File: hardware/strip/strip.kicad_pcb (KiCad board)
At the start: 4 copper layers, 66 x 18 mm, 43 parts, among them J105 CORTEX-DEBUG, J106 JAE_DX07S016JA3, J301 WAGO-2065, J302 WAGO-2065, J303 WAGO-2065, SW101 SW_Push, SW102 SW_Push, U102 ATSAMD51G, U103 AP2112K-3.3, U301 74AHC1G125, Y101 32k768

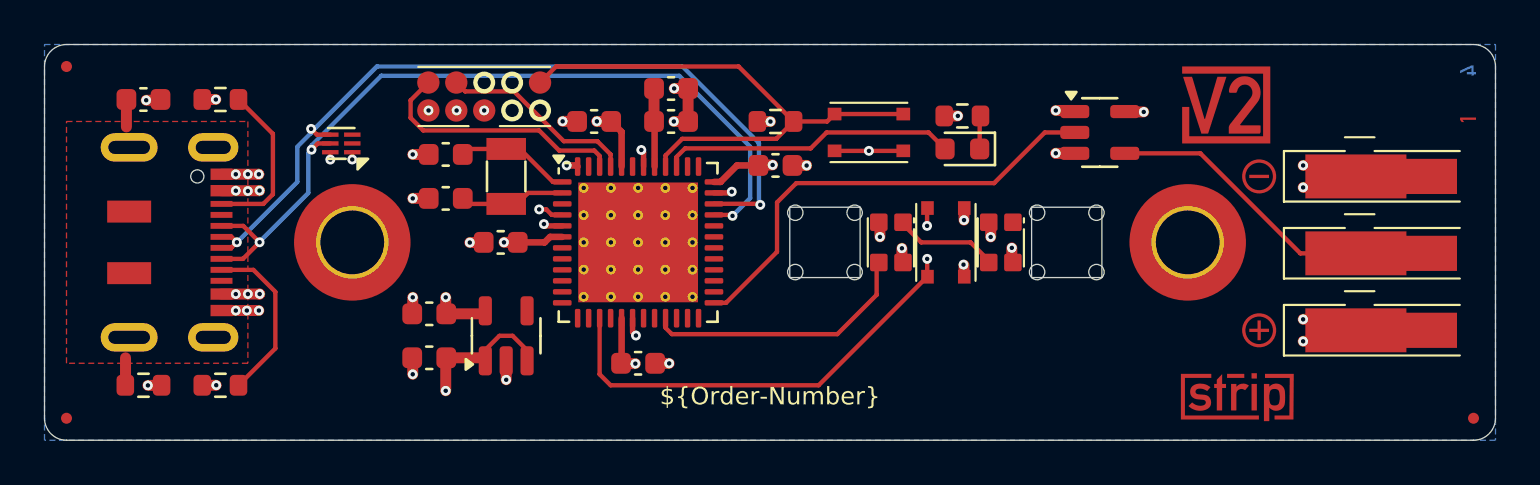
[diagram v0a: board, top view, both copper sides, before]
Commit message: Replace Order_Number
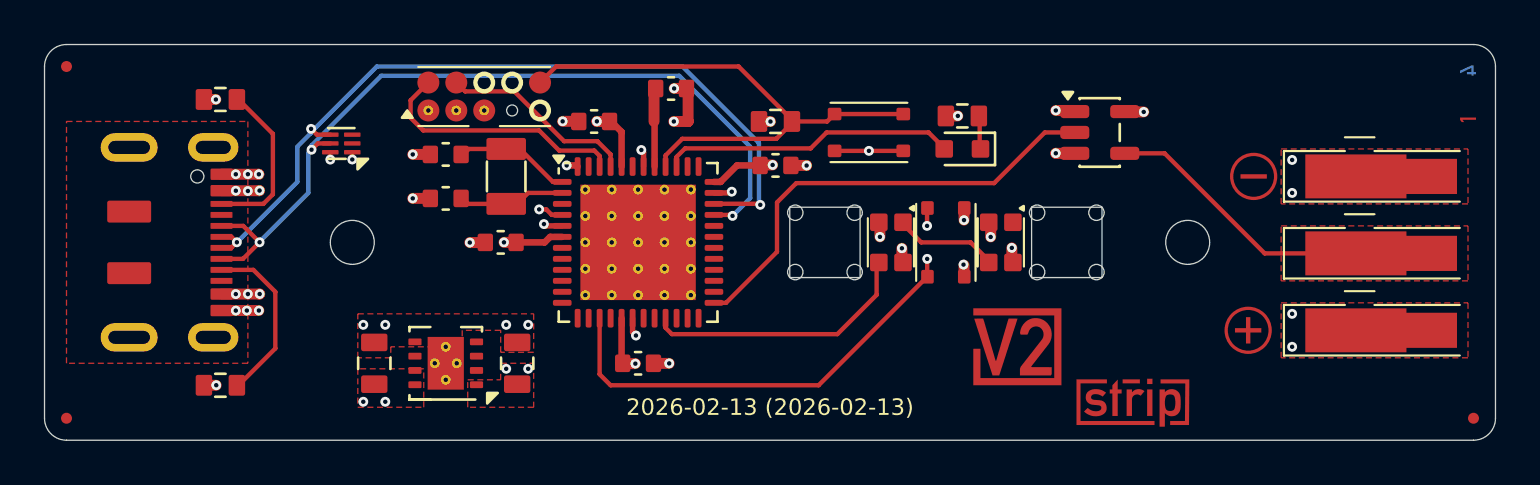
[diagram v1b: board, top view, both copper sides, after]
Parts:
- removed C104, C112: 0u1, Capacitor_SMD:C_0603_1608Metric
- removed C109, C110: 10u, Capacitor_SMD:C_0603_1608Metric
- removed R105: 1M, Resistor_SMD:R_0603_1608Metric
- removed SPACER101, SPACER102: 3mm, V2_Spacer_Wurth:9774030243
- removed U103: AP2112K-3.3, Package_TO_SOT_SMD:SOT-23-5
- added C1: 10u, V2_Capacitor_SMD:C_0805, F.Cu at (132.0, 111.5)
- added C2: 10u, V2_Capacitor_SMD:C_0805, F.Cu at (138.5, 111.5)
- added H101: 2mm, V2_Mechanical:MountingHole_2mm, F.Cu at (131.0, 106.0)
- added H102: 2mm, V2_Mechanical:MountingHole_2mm, F.Cu at (169.0, 106.0)
- added U101: TPS78433QWDRBRQ1, V2_Package_SON:VSON-8-1_3x3mm_P0.65_EP1.65x2.4mm, F.Cu at (135.2, 111.5)
- C101, C102, C103, C105, C106, C107, C108: footprint Capacitor_SMD:C_0603_1608Metric -> V2_Capacitor_SMD:C_0603
- D101: footprint LED_SMD:LED_0603_1608Metric -> V2_LED:LED_0603
- FID101, FID102, FID103: value Fiducial -> Fiducial_Paste
- INFO101: value ORDER-NUMBER -> ~; footprint V2_Production:Order_Number -> V2_Production:Revision
- J105: value CORTEX-DEBUG -> Cortex; footprint V2_Cortex_Debug:Cortex_Debug_Pad -> V2_Connector_Debug:Cortex
- J106: value JAE_DX07S016JA3 -> DX07S016JA3
- J301, J302, J303: value WAGO-2065 -> WAGO 2065-100
- R101, R102, R103, R104: footprint Resistor_SMD:R_0603_1608Metric -> V2_Resistor_SMD:R_0603
- SW101, SW102: value SW_Push -> SKSG
- U301: footprint Package_TO_SOT_SMD:SOT-23-5 -> V2_Package_TO_SOT_SMD:SOT-23-5
- moved ICON102 14.5 mm to (161.2, 110.8)
- moved ICON101 4.76 mm to (166.5, 113.2)
- moved ICON104 0.50 mm to (171.8, 110.0)
- moved INFO101 0.50 mm to (150.0, 113.5)
- moved ICON103 0.25 mm to (172.0, 103.0)
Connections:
- J106 pad S: Earth -> Shield
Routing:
- net +5V: track 18.0 -> 6.03 mm, vias 13 -> 14
- net GND: track 32.6 -> 23.8 mm, vias 39 -> 36
- net +3V3: track 15.7 -> 13.1 mm
- net Earth: track 2.50 -> 0.00 mm
- added copper zone on F.Cu, net +3V3
- added copper zone on F.Cu, net +5V
- added copper zone on F.Cu, net /LED Strip/WS2812-data
- added copper zone on F.Cu, net GND
- added copper zone on In2.Cu, net GND
- added copper zone on F.Cu, net Shield
- removed copper zone on B.Cu, net Earth
- removed copper zone on F.Cu, net Earth

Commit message: Update
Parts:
- renumbered C105 to C104, C106 to C105, C107 to C106, C108 to C107, C1 to C108, C2 to C109, J105 to J101, J106 to J102, J301 to J201, J302 to J202, J303 to J203, U102 to U101, U101 to U102, U301 to U201
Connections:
- net Shield renamed /Shield
